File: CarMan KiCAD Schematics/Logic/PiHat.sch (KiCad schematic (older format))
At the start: 11 parts, among them J7 Conn_01x02_Male, U2 ISO1050DUB, U8 MCP2515-xSO, Y1 16MHz

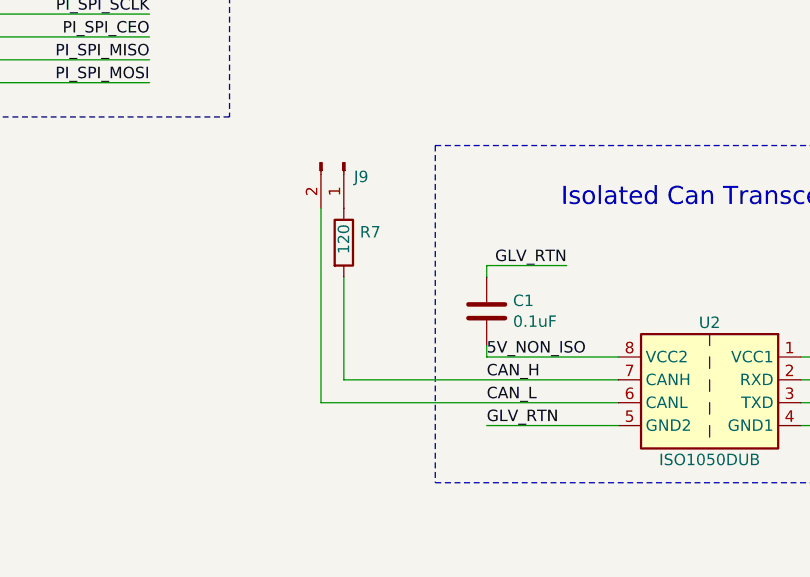
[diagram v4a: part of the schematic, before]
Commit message: - Adding J10 -> non isolated i2C testing header
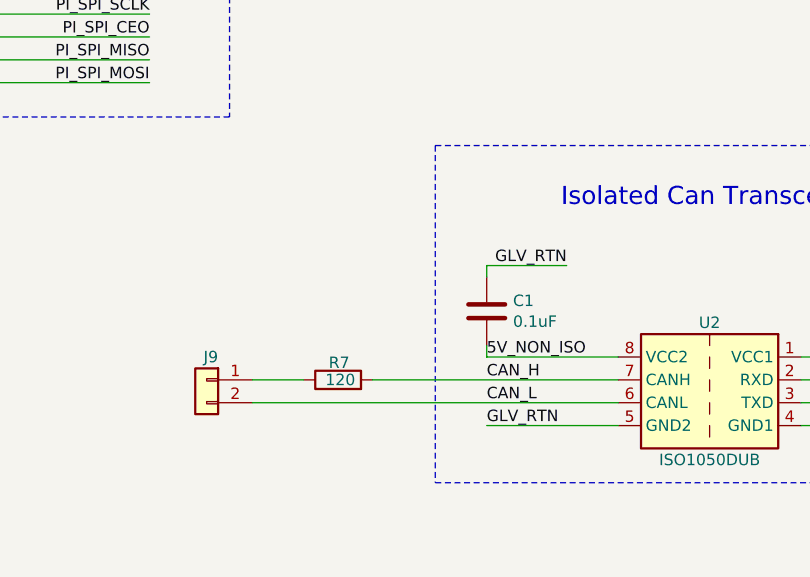
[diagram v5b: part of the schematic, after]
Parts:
- removed J7: Conn_01x02_Male, Connector_PinSocket_2.54mm:PinSocket_1x02_P2.54mm_Vertical, symbol Logic-rescue:Conn_01x02_Male-Connector-Logic-rescue
- added J9: IMU PS, Connector_PinSocket_2.54mm:PinSocket_1x02_P2.54mm_Vertical, symbol Connector_Generic:Conn_01x02
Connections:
- net CAN_L: now also J9.2 (Pin_2)
- net at R7.1: now also J9.1 (Pin_1)
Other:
- moved on the sheet: R7
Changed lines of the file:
@@
 ISO_RTN
-$Comp
-L Logic-rescue:Conn_01x02_Male-Connector-Logic-rescue J7
-U 1 1 5F9AE3B8
-P 2850 2575
-AR Path="/5F9AE3B8" Ref="J7"  Part="1"
-AR Path="/5F9A7CF0/5F9AE3B8" Ref="J9"  Part="1"
-F 0 "J9" V 2912 2619 50  0000 L CNN
-F 1 "Conn_01x02_Male" V 3050 1725 50  0001 L CNN
-F 2 "Connector_PinSocket_2.54mm:PinSocket_1x02_P2.54mm_Vertical" H 2850 2575 50  0001 C CNN
-F 3 "~" H 2850 2575 50  0001 C CNN
-	1    2850 2575
-	0    1    1    0
-$EndComp
 $Comp
 L Logic-rescue:R-Device-Logic-rescue R7
 U 1 1 5F9AF7D2
-P 2850 2925
+P 2825 3525
 AR Path="/5F9AF7D2" Ref="R7"  Part="1"
 AR Path="/5F9A7CF0/5F9AF7D2" Ref="R7"  Part="1"
-F 0 "R7" H 2920 2971 50  0000 L CNN
-F 1 "120" V 2850 2875 50  0000 L CNN
-F 2 "Resistor_SMD:R_0805_2012Metric_Pad1.15x1.40mm_HandSolder" V 2780 2925 50  0001 C CNN
-F 3 "~" H 2850 2925 50  0001 C CNN
-	1    2850 2925
-	1    0    0    -1
-$EndComp
-Wire Wire Line
-	2750 2775 2750 3625
+F 0 "R7" V 2900 3475 50  0000 L CNN
+F 1 "120" V 2825 3450 50  0000 L CNN
+F 2 "Resistor_SMD:R_0805_2012Metric_Pad1.15x1.40mm_HandSolder" V 2755 3525 50  0001 C CNN
+F 3 "~" H 2825 3525 50  0001 C CNN
+	1    2825 3525
+	0    -1   -1   0
+$EndComp
 Wire Wire Line
 	5425 3375 5425 3425
@@
 Wire Wire Line
 	1275 1075 1975 1075
-Wire Wire Line
-	2850 3075 2850 3525
 $Comp
 L Logic-rescue:ISO1050DUB-Interface_CAN_LIN-Logic-rescue U2
@@
 5V_ISO
 Wire Wire Line
-	2850 3525 4050 3525
-Wire Wire Line
-	2750 3625 4050 3625
-Wire Wire Line
 	3475 3425 4050 3425
 Text Label 3475 3425 0    50   ~ 0
@@
 Wire Notes Line
 	3250 2500 3250 3975
+$Comp
+L Connector_Generic:Conn_01x02 J?
+U 1 1 609288D9
+P 2250 3525
+AR Path="/609288D9" Ref="J?"  Part="1"
+AR Path="/5F9A7CF0/609288D9" Ref="J9"  Part="1"
+F 0 "J9" H 2200 3625 50  0000 L CNN
+F 1 "IMU PS" H 2100 3300 50  0001 L CNN
+F 2 "Connector_PinSocket_2.54mm:PinSocket_1x02_P2.54mm_Vertical" H 2250 3525 50  0001 C CNN
+F 3 "~" H 2250 3525 50  0001 C CNN
+	1    2250 3525
+	-1   0    0    -1
+$EndComp
+Wire Wire Line
+	2450 3625 4050 3625
+Wire Wire Line
+	2450 3525 2675 3525
+Wire Wire Line
+	2975 3525 4050 3525
 $EndSCHEMATC

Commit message: Logic updated
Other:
- note added: "NON-ISO CAN\nTesting Header"
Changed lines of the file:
@@
 Wire Wire Line
 	2975 3525 4050 3525
+Text Notes 2025 3875 0    47   ~ 0
+NON-ISO CAN\nTesting Header
 $EndSCHEMATC

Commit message: Updated TSI Schematic
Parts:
- J7: renamed from J9; value IMU PS -> NON-ISO CAN Testing
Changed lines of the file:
@@
 P 2250 3525
 AR Path="/609288D9" Ref="J?"  Part="1"
-AR Path="/5F9A7CF0/609288D9" Ref="J9"  Part="1"
-F 0 "J9" H 2200 3625 50  0000 L CNN
-F 1 "IMU PS" H 2100 3300 50  0001 L CNN
+AR Path="/5F9A7CF0/609288D9" Ref="J7"  Part="1"
+F 0 "J7" H 2200 3625 50  0000 L CNN
+F 1 "NON-ISO CAN Testing" H 2100 3300 50  0001 L CNN
 F 2 "Connector_PinSocket_2.54mm:PinSocket_1x02_P2.54mm_Vertical" H 2250 3525 50  0001 C CNN
 F 3 "~" H 2250 3525 50  0001 C CNN

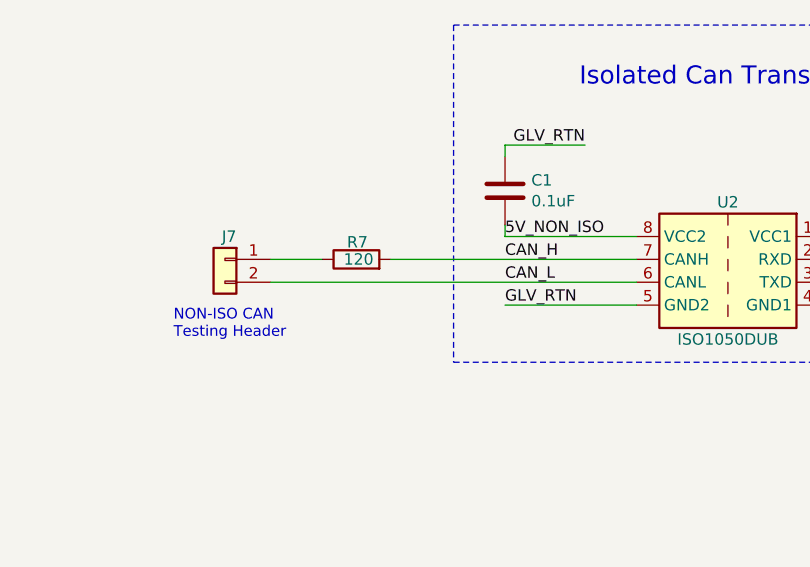
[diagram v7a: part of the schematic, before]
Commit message: Added Footprint for Pi RTC. organized board
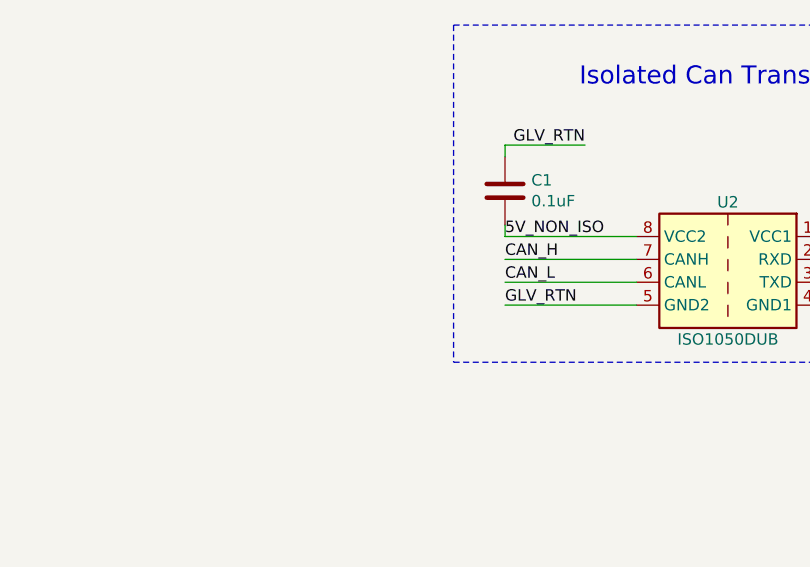
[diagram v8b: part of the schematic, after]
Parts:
- removed J7: NON-ISO CAN Testing, Connector_PinSocket_2.54mm:PinSocket_1x02_P2.54mm_Vertical, symbol Connector_Generic:Conn_01x02
- removed R7: 120, Resistor_SMD:R_0805_2012Metric_Pad1.15x1.40mm_HandSolder, symbol Logic-rescue:R-Device-Logic-rescue
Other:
- note removed: "NON-ISO CAN\nTesting Header"
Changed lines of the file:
@@
 Text Label 2000 1725 2    50   ~ 0
 ISO_RTN
-$Comp
-L Logic-rescue:R-Device-Logic-rescue R7
-U 1 1 5F9AF7D2
-P 2825 3525
-AR Path="/5F9AF7D2" Ref="R7"  Part="1"
-AR Path="/5F9A7CF0/5F9AF7D2" Ref="R7"  Part="1"
-F 0 "R7" V 2900 3475 50  0000 L CNN
-F 1 "120" V 2825 3450 50  0000 L CNN
-F 2 "Resistor_SMD:R_0805_2012Metric_Pad1.15x1.40mm_HandSolder" V 2755 3525 50  0001 C CNN
-F 3 "~" H 2825 3525 50  0001 C CNN
-	1    2825 3525
-	0    -1   -1   0
-$EndComp
 Wire Wire Line
 	5425 3375 5425 3425
@@
 Wire Notes Line
 	3250 2500 3250 3975
-$Comp
-L Connector_Generic:Conn_01x02 J?
-U 1 1 609288D9
-P 2250 3525
-AR Path="/609288D9" Ref="J?"  Part="1"
-AR Path="/5F9A7CF0/609288D9" Ref="J7"  Part="1"
-F 0 "J7" H 2200 3625 50  0000 L CNN
-F 1 "NON-ISO CAN Testing" H 2100 3300 50  0001 L CNN
-F 2 "Connector_PinSocket_2.54mm:PinSocket_1x02_P2.54mm_Vertical" H 2250 3525 50  0001 C CNN
-F 3 "~" H 2250 3525 50  0001 C CNN
-	1    2250 3525
-	-1   0    0    -1
-$EndComp
-Wire Wire Line
-	2450 3625 4050 3625
-Wire Wire Line
-	2450 3525 2675 3525
-Wire Wire Line
-	2975 3525 4050 3525
-Text Notes 2025 3875 0    47   ~ 0
-NON-ISO CAN\nTesting Header
+Wire Wire Line
+	3475 3525 4050 3525
+Wire Wire Line
+	3475 3625 4050 3625
 $EndSCHEMATC
